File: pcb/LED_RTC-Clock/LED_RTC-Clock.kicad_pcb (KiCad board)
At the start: 2 copper layers, 35.6 x 66 mm, 5 parts, among them J1 Jack_DC_5V, J2 LED_Matrix, J3 LED_DC, J4 RTC

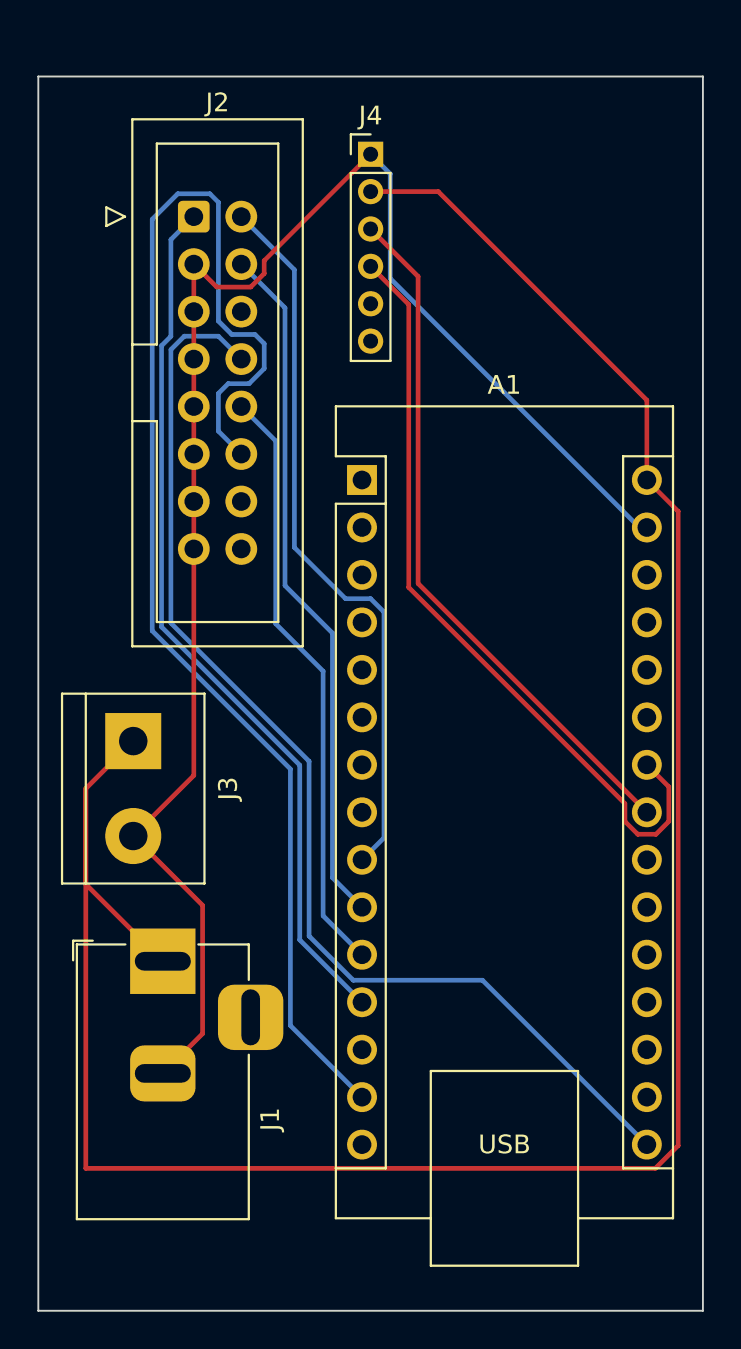
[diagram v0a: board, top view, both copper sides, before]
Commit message: Updated PCB and Schematic
Updated the PCB and schematics to add a potentiometer for brightness control. Also tidied up traces, modified silkscreens and finalised board layout. Silkscreened V1.0
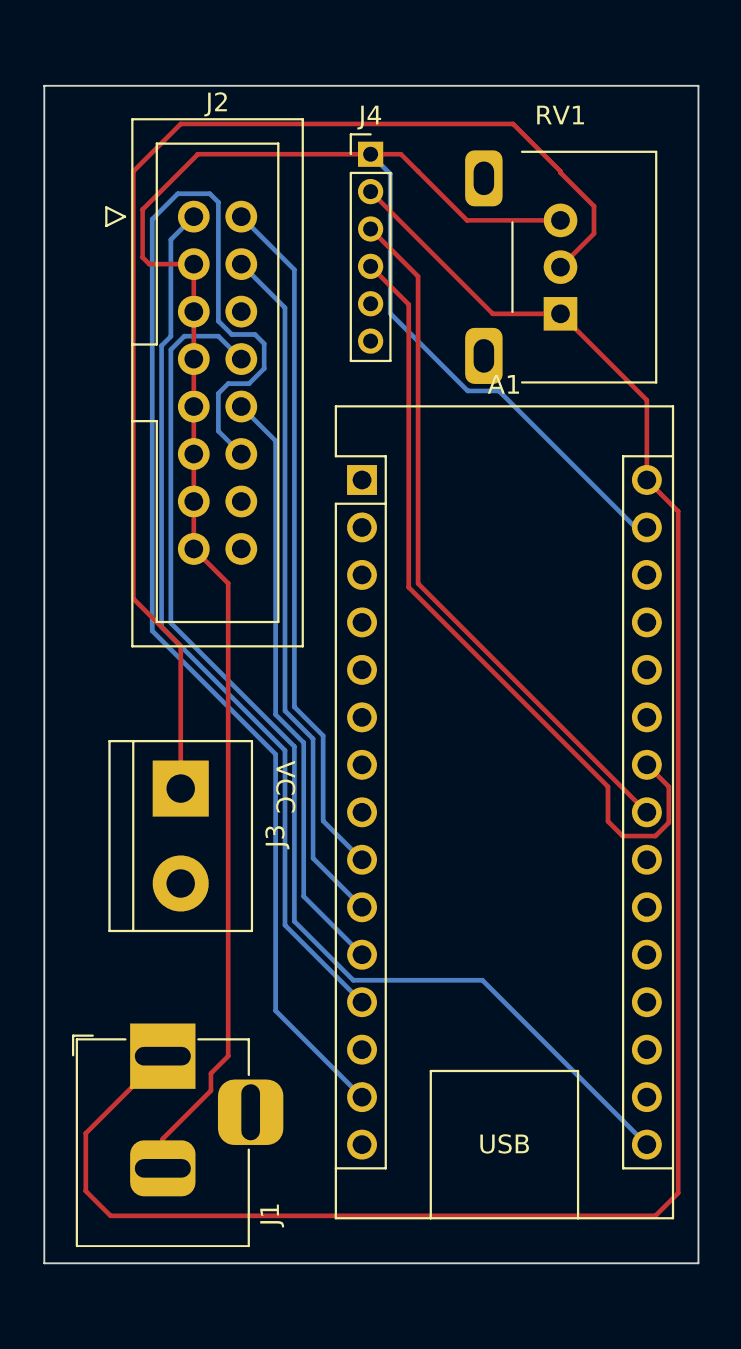
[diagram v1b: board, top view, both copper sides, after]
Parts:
- added RV1: R_Potentiometer, Potentiometer_THT:Potentiometer_Alps_RK09L_Single_Horizontal, F.Cu at (134.6, 76.2)
- moved J1 5.08 mm to (113.3, 115.9)
- moved J3 3.59 mm to (114.3, 101.6)
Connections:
- J3 pad 1: Net-(A1-VIN) -> Net-(J3-Pin_1)
- J3 pad 2: Net-(J2-A) -> unconnected-(J3-Pin_2-Pad2)
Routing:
- net Net-(J3-Pin_1): track 0.00 -> 65.6 mm
- net Net-(A1-VIN): track 127.0 -> 104.2 mm
- net Net-(J2-A): track 86.7 -> 108.5 mm
- net Net-(A1-D6): track 38.8 -> 37.1 mm
- net Net-(A1-A5): track 41.8 -> 42.4 mm
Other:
- board size 35.6 x 66 mm -> 35 x 63 mm
- board text added: "LED_RTC-Clock V1.0 Created by Harrison Asmar"

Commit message: Updated PCB to V1.1
I received the manufactured PCBs and found that I had selected the incorrect pin spacing for the RTC header. Updated the Pin spacing from 2mm to 2.54mm and re-routed the affected traces.
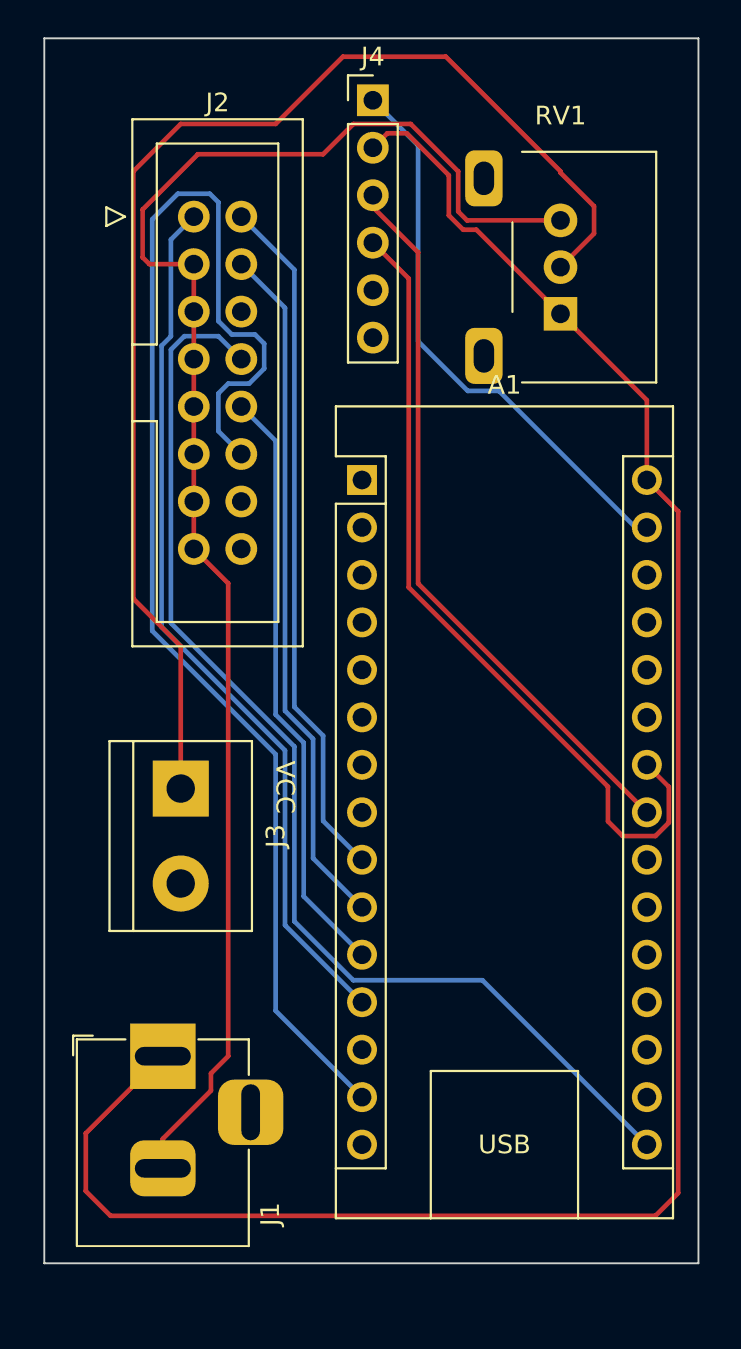
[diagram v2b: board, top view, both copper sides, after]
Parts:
- J4: footprint Connector_PinHeader_2.00mm:PinHeader_1x06_P2.00mm_Vertical -> Connector_PinHeader_2.54mm:PinHeader_1x06_P2.54mm_Vertical
- moved J4 2.89 mm to (124.6, 64.8)
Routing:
- net Net-(J2-A): track 108.5 -> 114.0 mm
- net Net-(J3-Pin_1): track 65.6 -> 68.6 mm
- net Net-(A1-VIN): track 104.2 -> 106.9 mm
- net Net-(A1-A4): track 37.3 -> 39.1 mm
- net Net-(A1-A5): track 42.4 -> 43.6 mm
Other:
- board size 35 x 63 mm -> 35 x 65.5 mm
- board text added: "LED_RTC-Clock V1.1 Created by Harrison Asmar"
- board text removed: "LED_RTC-Clock V1.0 Created by Harrison Asmar"
